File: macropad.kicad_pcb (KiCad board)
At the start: 2 copper layers, 96.3 x 99 mm, 37 parts, among them SW1 RotaryEncoder_Switch, U1 MOUDLE-SEEEDUINO-XIAO

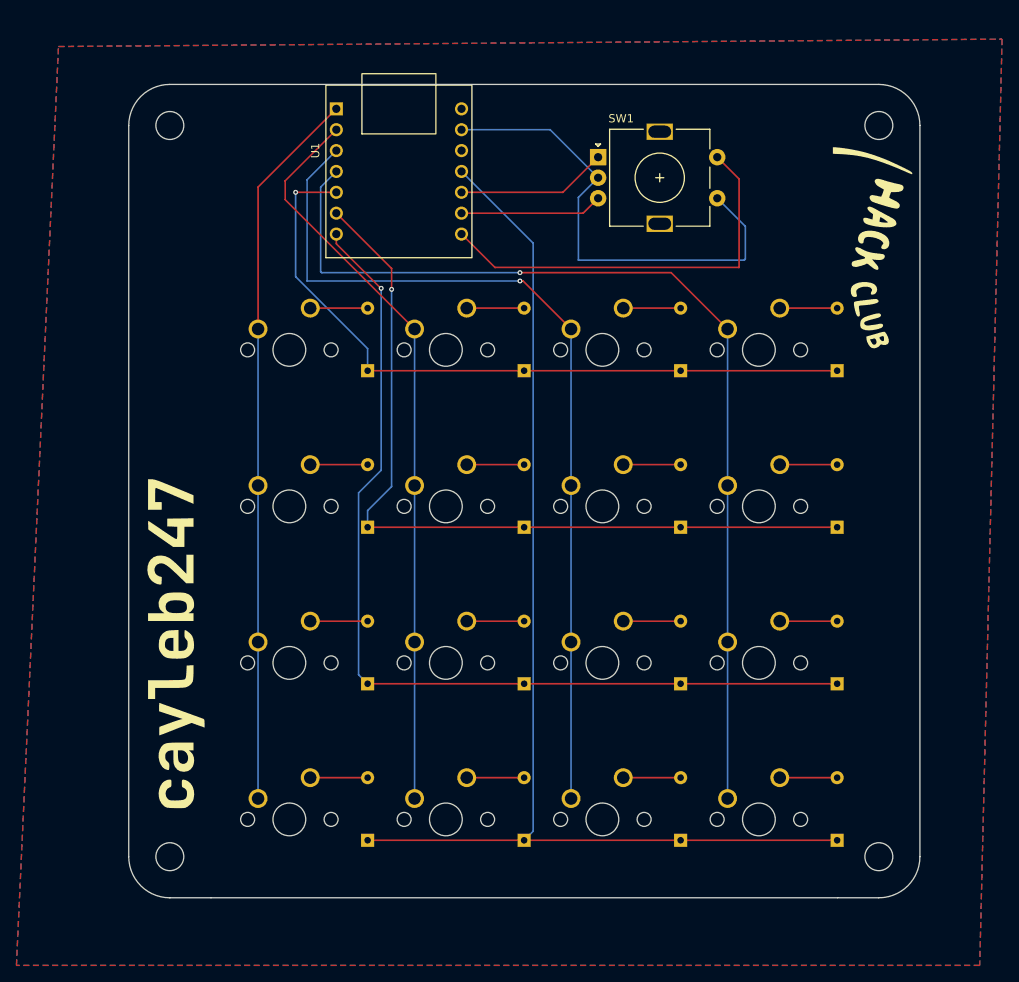
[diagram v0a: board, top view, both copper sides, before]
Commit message: Rewire PCB with MCU on back
Also centered the rotary encoder swtich
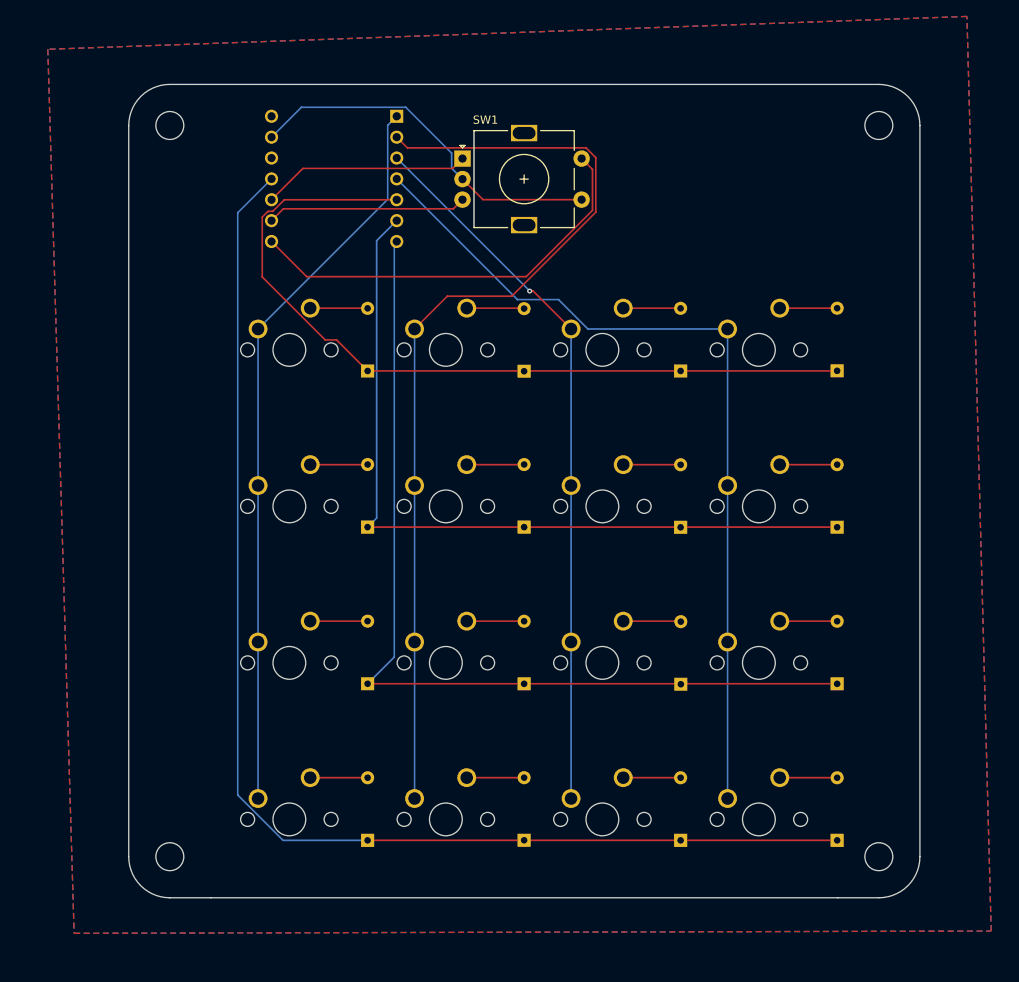
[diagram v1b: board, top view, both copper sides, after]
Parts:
- removed the G*** at (70.8, 119.2)
- removed the G*** at (155.7, 73.0)
- added G***: LOGO, graphics:seal_small, B.Cu at (137.6, 62.4)
- U1: moved to B.Cu
- moved D1 57.2 mm to (94.1, 85.9)
- moved D19 57.2 mm to (94.1, 104.9)
- moved D18 57.2 mm to (151.2, 85.9)
- moved D26 57.2 mm to (151.2, 124.0)
- moved D27 57.2 mm to (94.1, 143.0)
- moved D30 57.2 mm to (151.2, 143.0)
- moved D22 57.1 mm to (151.2, 104.9)
- moved D23 57.1 mm to (94.1, 124.0)
- moved D25 19.1 mm to (132.2, 124.0)
- moved D16 19.1 mm to (113.1, 85.9)
- moved D17 19.1 mm to (132.2, 85.9)
- moved D20 19.1 mm to (113.1, 104.9)
- moved D21 19.1 mm to (132.2, 104.9)
- moved D24 19.1 mm to (113.1, 124.0)
- moved D29 19.1 mm to (132.2, 143.0)
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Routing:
- net COL1: track 90.5 -> 117.0 mm
- net COL2: track 109.0 -> 87.0 mm
- net COL3: track 122.6 -> 105.0 mm, vias 1 -> 0
- net GND: track 59.3 -> 45.0 mm
- net ROW0: track 87.4 -> 99.2 mm, vias 1 -> 0
- net ROW3: track 142.6 -> 151.9 mm
- net EC11A: track 18.4 -> 25.3 mm
- net EC11B: track 17.4 -> 24.3 mm
- net ROW1: track 99.4 -> 95.9 mm, vias 1 -> 0
- net ROW2: track 115.8 -> 112.5 mm, vias 1 -> 0
- net COL0: track 87.9 -> 90.0 mm
- net EC11SW: track 50.0 -> 51.0 mm
- added copper zone on B.Cu, net (none)
- added copper zone on F.Cu, net (none)
- removed copper zone on B.Cu, net COL1
- removed copper zone on F.Cu, net COL1

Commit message: Remove screw holes
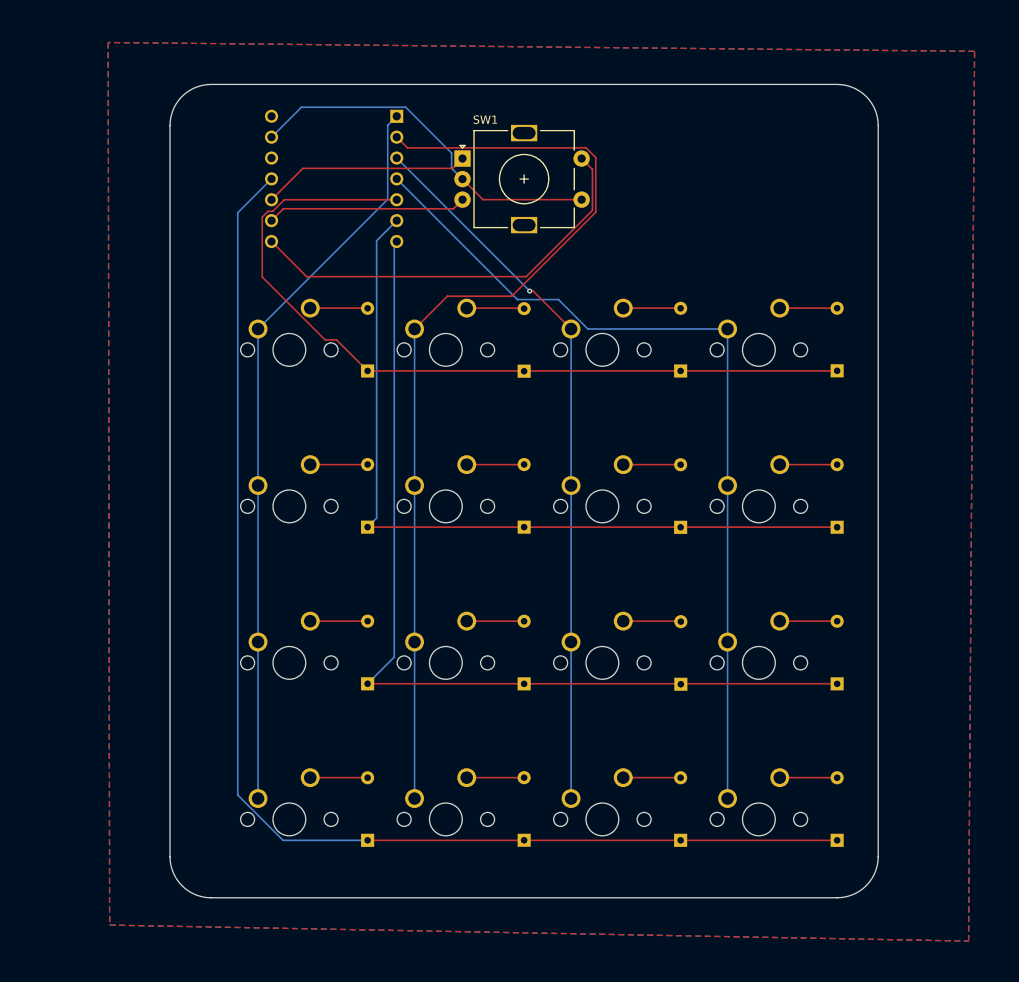
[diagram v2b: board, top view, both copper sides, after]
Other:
- board size 96.3 x 99 mm -> 86.2 x 99 mm
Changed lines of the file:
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@@
 		)
 	)
-	(gr_circle
-		(center 70 145)
-		(end 71.7 145)
+	(gr_line
+		(start 156.225 145)
+		(end 156.225 56)
 		(stroke
 			(width 0.05)
 			(type default)
 		)
-		(fill none)
 		(layer "Edge.Cuts")
 	)
 	(gr_line
-		(start 161.3 145)
-		(end 161.3 56)
+		(start 151.225 150)
+		(end 75.025 150)
 		(stroke
 			(width 0.05)
@@
 		(layer "Edge.Cuts")
 	)
-	(gr_line
-		(start 65 145)
-		(end 65 56)
+	(gr_arc
+		(start 70.025 56)
+		(mid 71.489466 52.464466)
+		(end 75.025 51)
 		(stroke
 			(width 0.05)
@@
 	)
 	(gr_arc
-		(start 65 56)
-		(mid 66.464466 52.464466)
-		(end 70 51)
+		(start 75.025 150)
+		(mid 71.489466 148.535534)
+		(end 70.025 145)
 		(stroke
 			(width 0.05)
@@
 		(layer "Edge.Cuts")
 	)
-	(gr_circle
-		(center 156.3 56)
-		(end 158 56)
+	(gr_line
+		(start 70.025 145)
+		(end 70.025 56)
 		(stroke
 			(width 0.05)
 			(type default)
 		)
-		(fill none)
 		(layer "Edge.Cuts")
 	)
-	(gr_line
-		(start 156.3 51)
-		(end 70 51)
+	(gr_arc
+		(start 156.225 145)
+		(mid 154.760534 148.535534)
+		(end 151.225 150)
 		(stroke
 			(width 0.05)
@@
 	)
 	(gr_line
-		(start 151.3 150)
-		(end 75 150)
+		(start 75.025 51)
+		(end 151.225 51)
 		(stroke
 			(width 0.05)
@@
 		(layer "Edge.Cuts")
 	)
-	(gr_circle
-		(center 156.3 145)
-		(end 158 145)
+	(gr_arc
+		(start 151.225 51)
+		(mid 154.760534 52.464466)
+		(end 156.225 56)
 		(stroke
 			(width 0.05)
 			(type default)
 		)
-		(fill none)
-		(layer "Edge.Cuts")
-	)
-	(gr_arc
-		(start 70 150)
-		(mid 66.464466 148.535534)
-		(end 65 145)
-		(stroke
-			(width 0.05)
-			(type default)
-		)
-		(layer "Edge.Cuts")
-	)
-	(gr_arc
-		(start 156.3 51)
-		(mid 159.835534 52.464466)
-		(end 161.3 56)
-		(stroke
-			(width 0.05)
-			(type default)
-		)
-		(layer "Edge.Cuts")
-	)
-	(gr_line
-		(start 151.3 150)
-		(end 156.3 150)
-		(stroke
-			(width 0.05)
-			(type default)
-		)
-		(layer "Edge.Cuts")
-	)
-	(gr_line
-		(start 75 150)
-		(end 70 150)
-		(stroke
-			(width 0.05)
-			(type default)
-		)
-		(layer "Edge.Cuts")
-	)
-	(gr_arc
-		(start 161.3 145)
-		(mid 159.835534 148.535534)
-		(end 156.3 150)
-		(stroke
-			(width 0.05)
-			(type default)
-		)
-		(layer "Edge.Cuts")
-	)
-	(gr_circle
-		(center 70 56)
-		(end 71.7 56)
-		(stroke
-			(width 0.05)
-			(type default)
-		)
-		(fill none)
 		(layer "Edge.Cuts")
 	)
@@
 		(polygon
 			(pts
-				(xy 55.15 46.725) (xy 58.35 154.325) (xy 169.975 154.05) (xy 167.025 42.725)
+				(xy 62.5 45.9) (xy 62.675 153.325) (xy 167.225 155.275) (xy 167.95 46.975)
 			)
 		)
